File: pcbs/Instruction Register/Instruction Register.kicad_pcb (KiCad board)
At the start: 2 copper layers, 38 parts, among them J1001 Conn_02x20_Odd_Even, J1002 Conn_02x20_Odd_Even, U1001 74HC245, U1002 74HC245, U1003 74HC245, U1004 74HC245, U2001 74HC14, U2002 74HC08, U2003 74HC138, U3001 74HC245

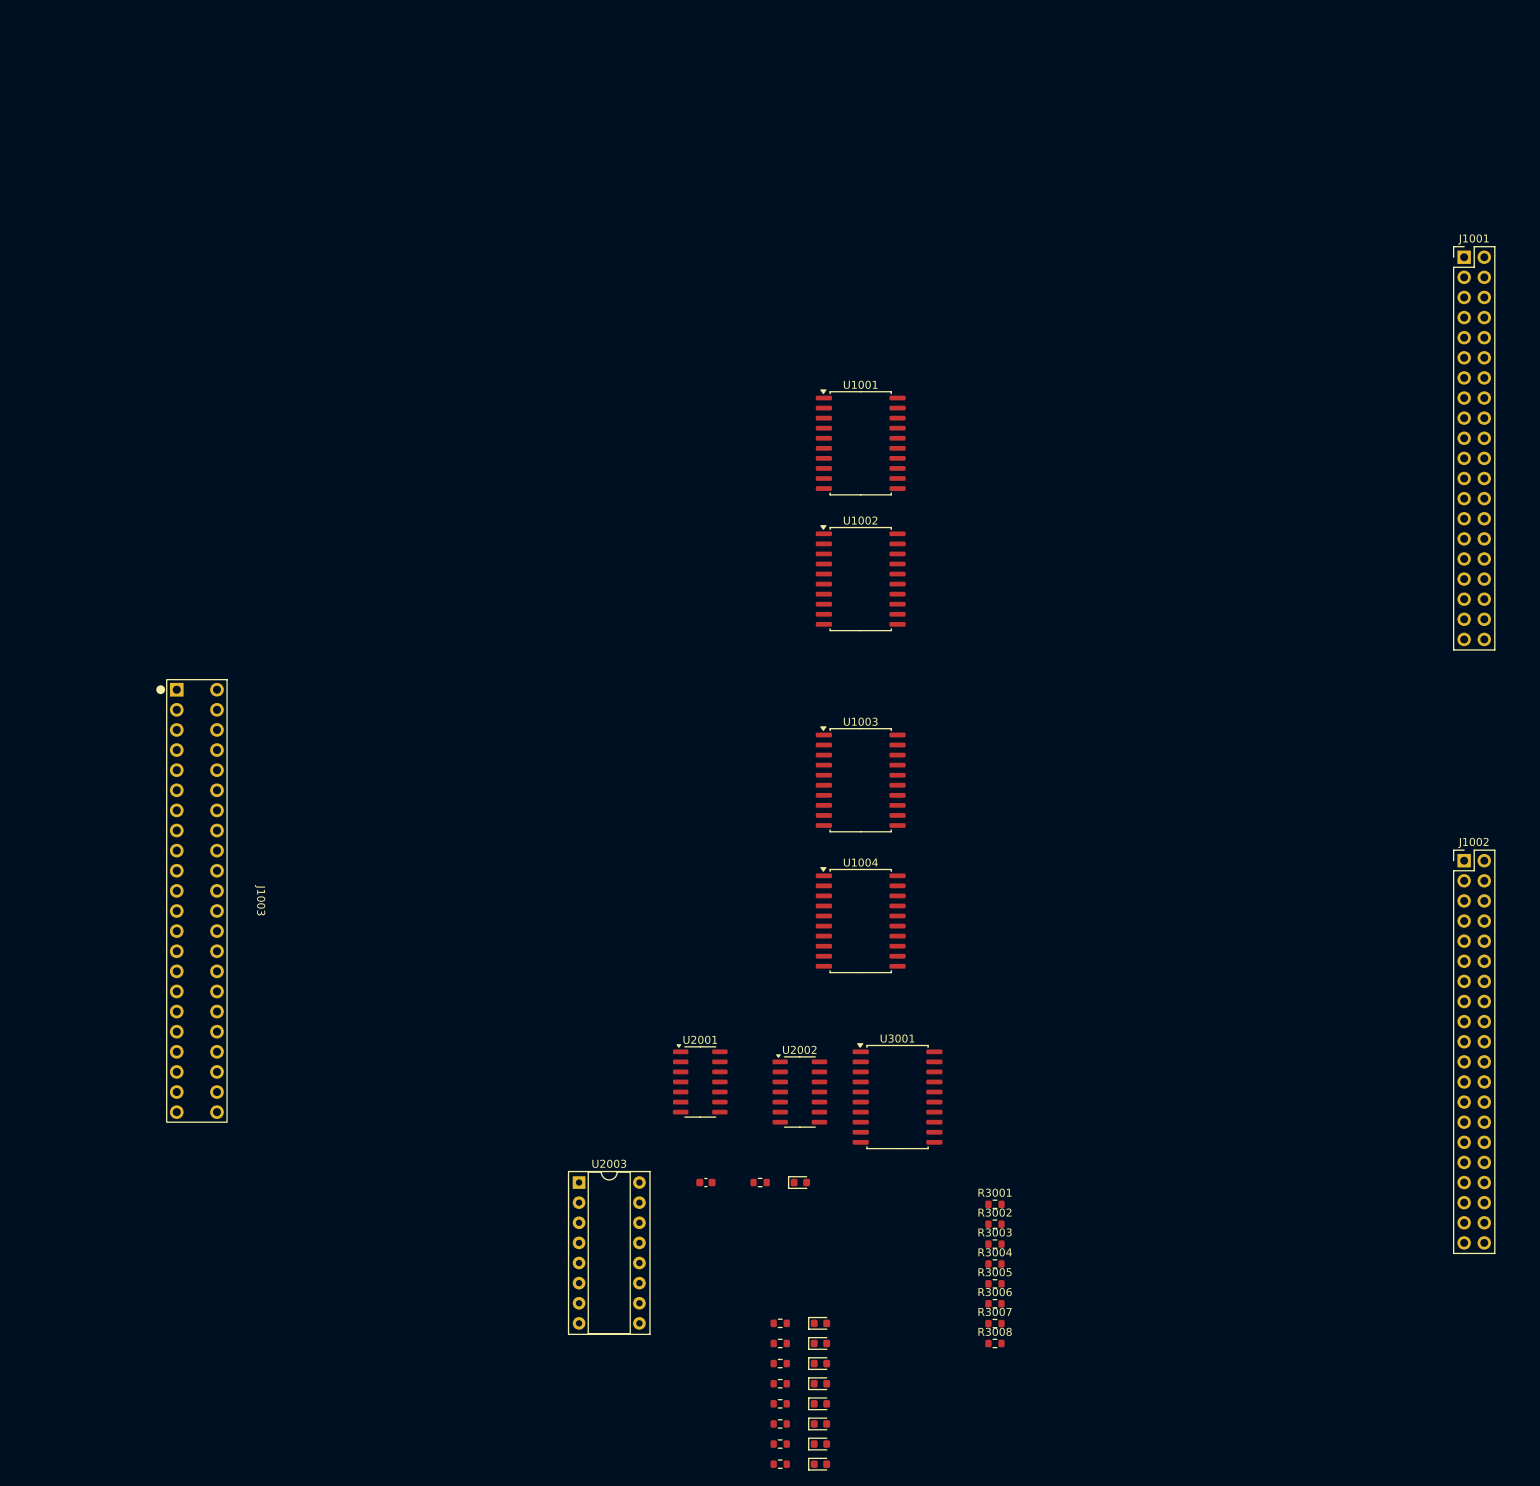
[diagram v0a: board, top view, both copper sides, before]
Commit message: Tweaking schematic and basic routing
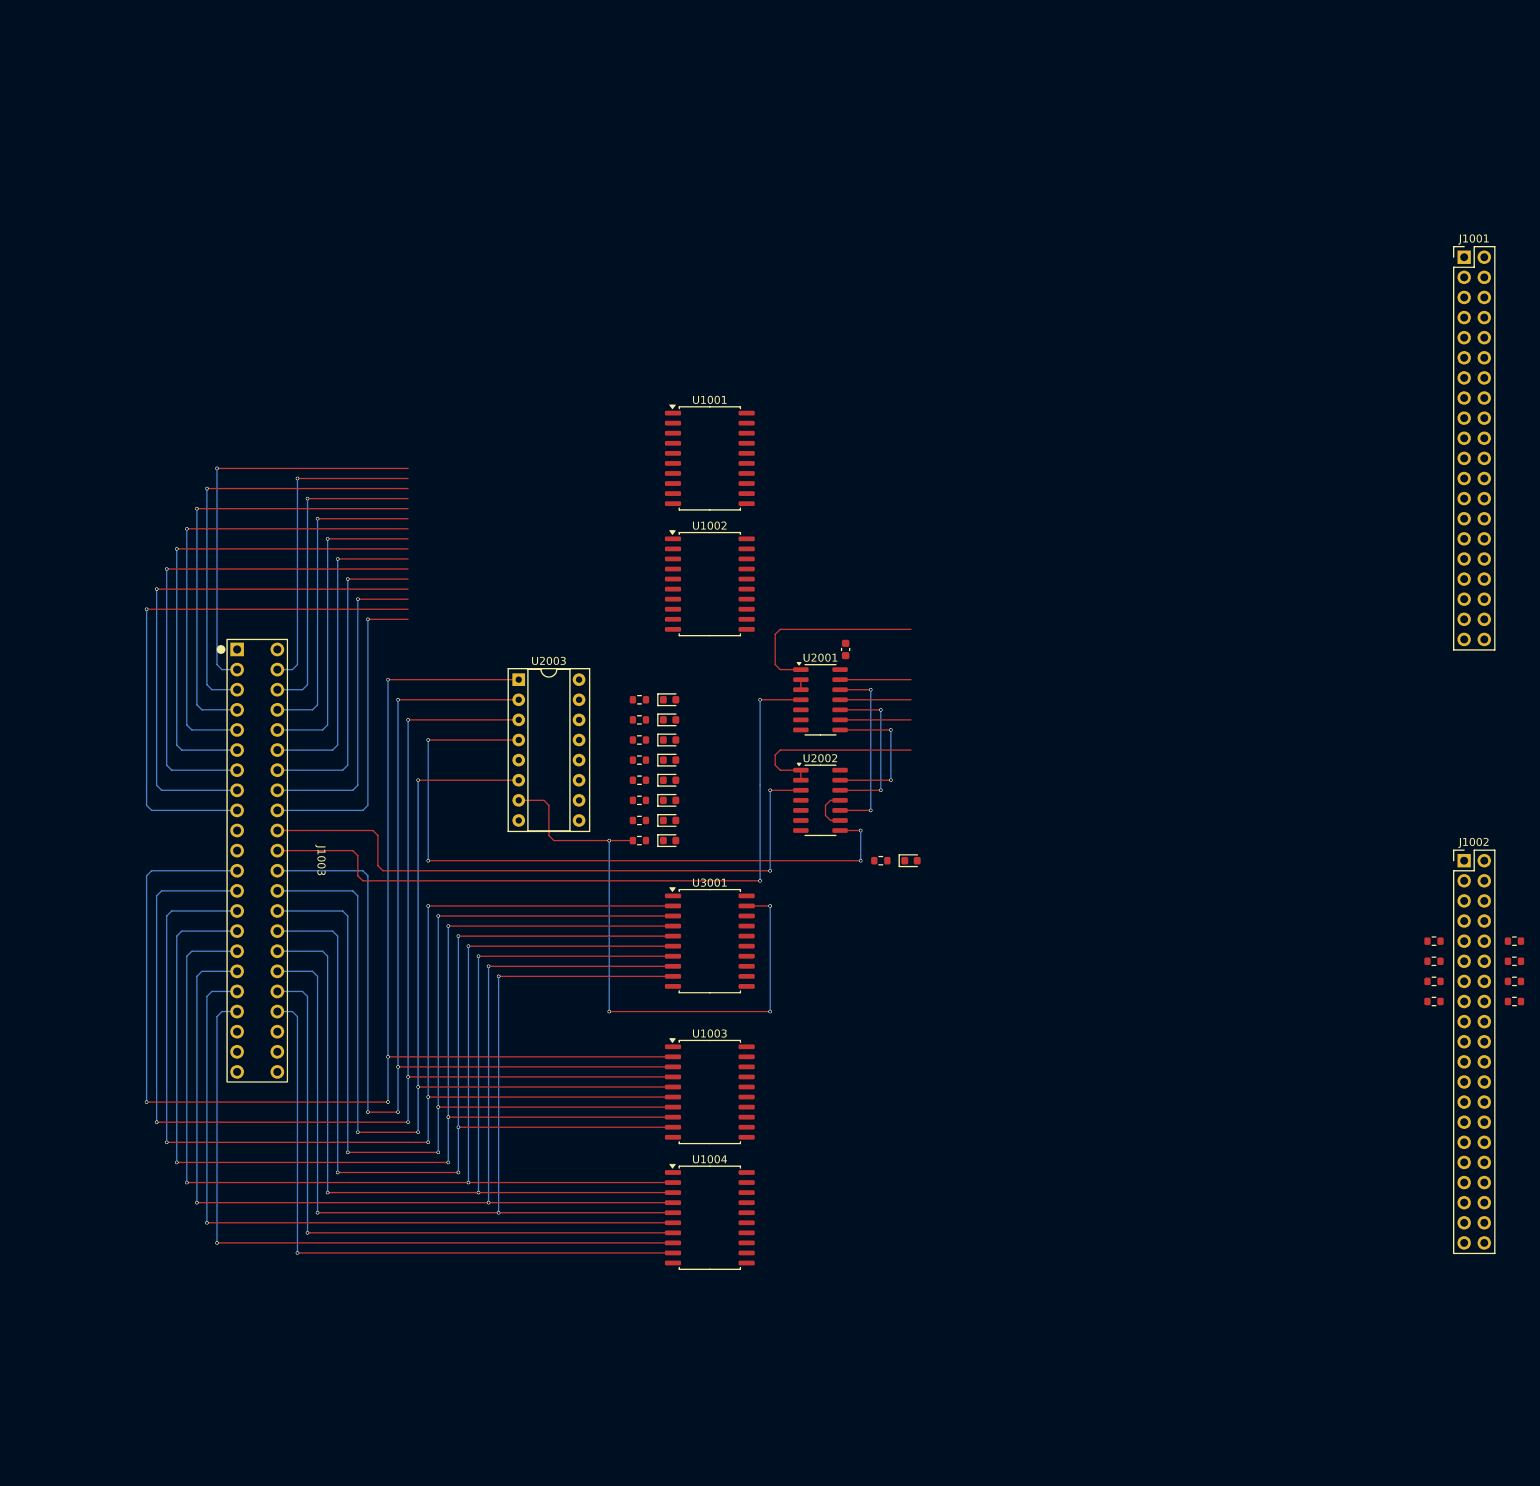
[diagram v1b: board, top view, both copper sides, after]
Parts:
- moved D2003 81.0 mm to (153.7, 109.2)
- moved D2006 81.0 mm to (153.7, 116.8)
- moved D2007 81.0 mm to (153.7, 119.4)
- moved D2004 81.0 mm to (153.7, 111.8)
- moved D2005 81.0 mm to (153.7, 114.3)
- moved D2008 81.0 mm to (153.7, 121.9)
- moved D2009 81.0 mm to (153.7, 124.5)
- moved D2002 81.0 mm to (153.7, 106.7)
- moved R2003 80.7 mm to (149.9, 109.2)
- moved R2006 80.7 mm to (149.9, 116.8)
- moved R2007 80.7 mm to (149.9, 119.4)
- moved R2004 80.7 mm to (149.9, 111.8)
- moved R2005 80.7 mm to (149.9, 114.3)
- moved R2008 80.7 mm to (149.9, 121.9)
- moved R2009 80.7 mm to (149.9, 124.5)
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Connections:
- J1003 pad B10: /~{RESET} -> /~{RESET}_{conn}
- U1001 pad 3: unconnected-(U1001-A1-Pad3) -> /Instr.In1
- U1001 pad 4: unconnected-(U1001-A2-Pad4) -> /Instr.In2
- U1001 pad 5: unconnected-(U1001-A3-Pad5) -> /Instr.In3
- U1001 pad 6: unconnected-(U1001-A4-Pad6) -> /Instr.In4
- U1001 pad 7: unconnected-(U1001-A5-Pad7) -> /Instr.In5
- U1001 pad 8: unconnected-(U1001-A6-Pad8) -> /Instr.In6
- U1001 pad 9: unconnected-(U1001-A7-Pad9) -> /Instr.In7
- U1002 pad 3: unconnected-(U1002-A1-Pad3) -> /Instr.In9
- U1002 pad 4: unconnected-(U1002-A2-Pad4) -> /Instr.In10
- U1002 pad 5: unconnected-(U1002-A3-Pad5) -> /Instr.In11
- U1002 pad 6: unconnected-(U1002-A4-Pad6) -> /Instr.In12
- U1002 pad 7: unconnected-(U1002-A5-Pad7) -> /Instr.In13
- U1002 pad 8: unconnected-(U1002-A6-Pad8) -> /Instr.In14
- U1002 pad 9: unconnected-(U1002-A7-Pad9) -> /Instr.In15
- U1003 pad 3: unconnected-(U1003-A1-Pad3) -> /Instr.Out1
- U1003 pad 4: unconnected-(U1003-A2-Pad4) -> /Instr.Out2
- U1003 pad 5: unconnected-(U1003-A3-Pad5) -> /Instr.Out3
- U1003 pad 6: unconnected-(U1003-A4-Pad6) -> /Instr.Out4
- U1003 pad 7: unconnected-(U1003-A5-Pad7) -> /Instr.Out5
- U1003 pad 8: unconnected-(U1003-A6-Pad8) -> /Instr.Out6
- U1003 pad 9: unconnected-(U1003-A7-Pad9) -> /Instr.Out7
- U1004 pad 3: unconnected-(U1004-A1-Pad3) -> /Instr.Out9
- U1004 pad 4: unconnected-(U1004-A2-Pad4) -> /Instr.Out10
- U1004 pad 5: unconnected-(U1004-A3-Pad5) -> /Instr.Out11
- U1004 pad 6: unconnected-(U1004-A4-Pad6) -> /Instr.Out12
- U1004 pad 7: unconnected-(U1004-A5-Pad7) -> /Instr.Out13
- U1004 pad 8: unconnected-(U1004-A6-Pad8) -> /Instr.Out14
- U1004 pad 9: unconnected-(U1004-A7-Pad9) -> /Instr.Out15
- U2002 pad 1: GND -> /~{RESET}
- U2002 pad 2: GND -> /~{RESET}
- U2002 pad 3: unconnected-(U2002-Pad3) -> /~{RESET}_{conn}
- U3001 pad 11: unconnected-(U3001-B7-Pad11) -> /C7
- U3001 pad 12: unconnected-(U3001-B6-Pad12) -> /C6
- U3001 pad 13: unconnected-(U3001-B5-Pad13) -> /C5
- U3001 pad 14: unconnected-(U3001-B4-Pad14) -> /C4
- U3001 pad 15: unconnected-(U3001-B3-Pad15) -> /C3
- U3001 pad 16: unconnected-(U3001-B2-Pad16) -> /C2
- U3001 pad 17: unconnected-(U3001-B1-Pad17) -> /C1
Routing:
- net /Instr.Out0: track 0.00 -> 176.6 mm, vias 0 -> 4
- net /Instr.Out2: track 0.00 -> 169.0 mm, vias 0 -> 4
- net /Instr.Out4: track 0.00 -> 162.4 mm, vias 0 -> 4
- net /Instr.Out6: track 0.00 -> 157.3 mm, vias 0 -> 4
- net /Instr.Out8: track 0.00 -> 152.3 mm, vias 0 -> 3
- net /Instr.Out1: track 0.00 -> 147.4 mm, vias 0 -> 4
- net /Instr.Out10: track 0.00 -> 147.2 mm, vias 0 -> 3
- net /Instr.Out5: track 0.00 -> 139.6 mm, vias 0 -> 4
- net /Instr.Out3: track 0.00 -> 137.2 mm, vias 0 -> 4
- net /Instr.Out7: track 0.00 -> 137.0 mm, vias 0 -> 4
- net /Instr.Out9: track 0.00 -> 134.5 mm, vias 0 -> 3
- net /Instr.Out11: track 0.00 -> 131.9 mm, vias 0 -> 3
- net /ClockInstr: track 0.00 -> 92.0 mm, vias 0 -> 2
- net /Instr.Out12: track 0.00 -> 91.5 mm, vias 0 -> 1
- net /Instr.Out14: track 0.00 -> 89.0 mm, vias 0 -> 1
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
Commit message: Completing routing; needs silkscreen
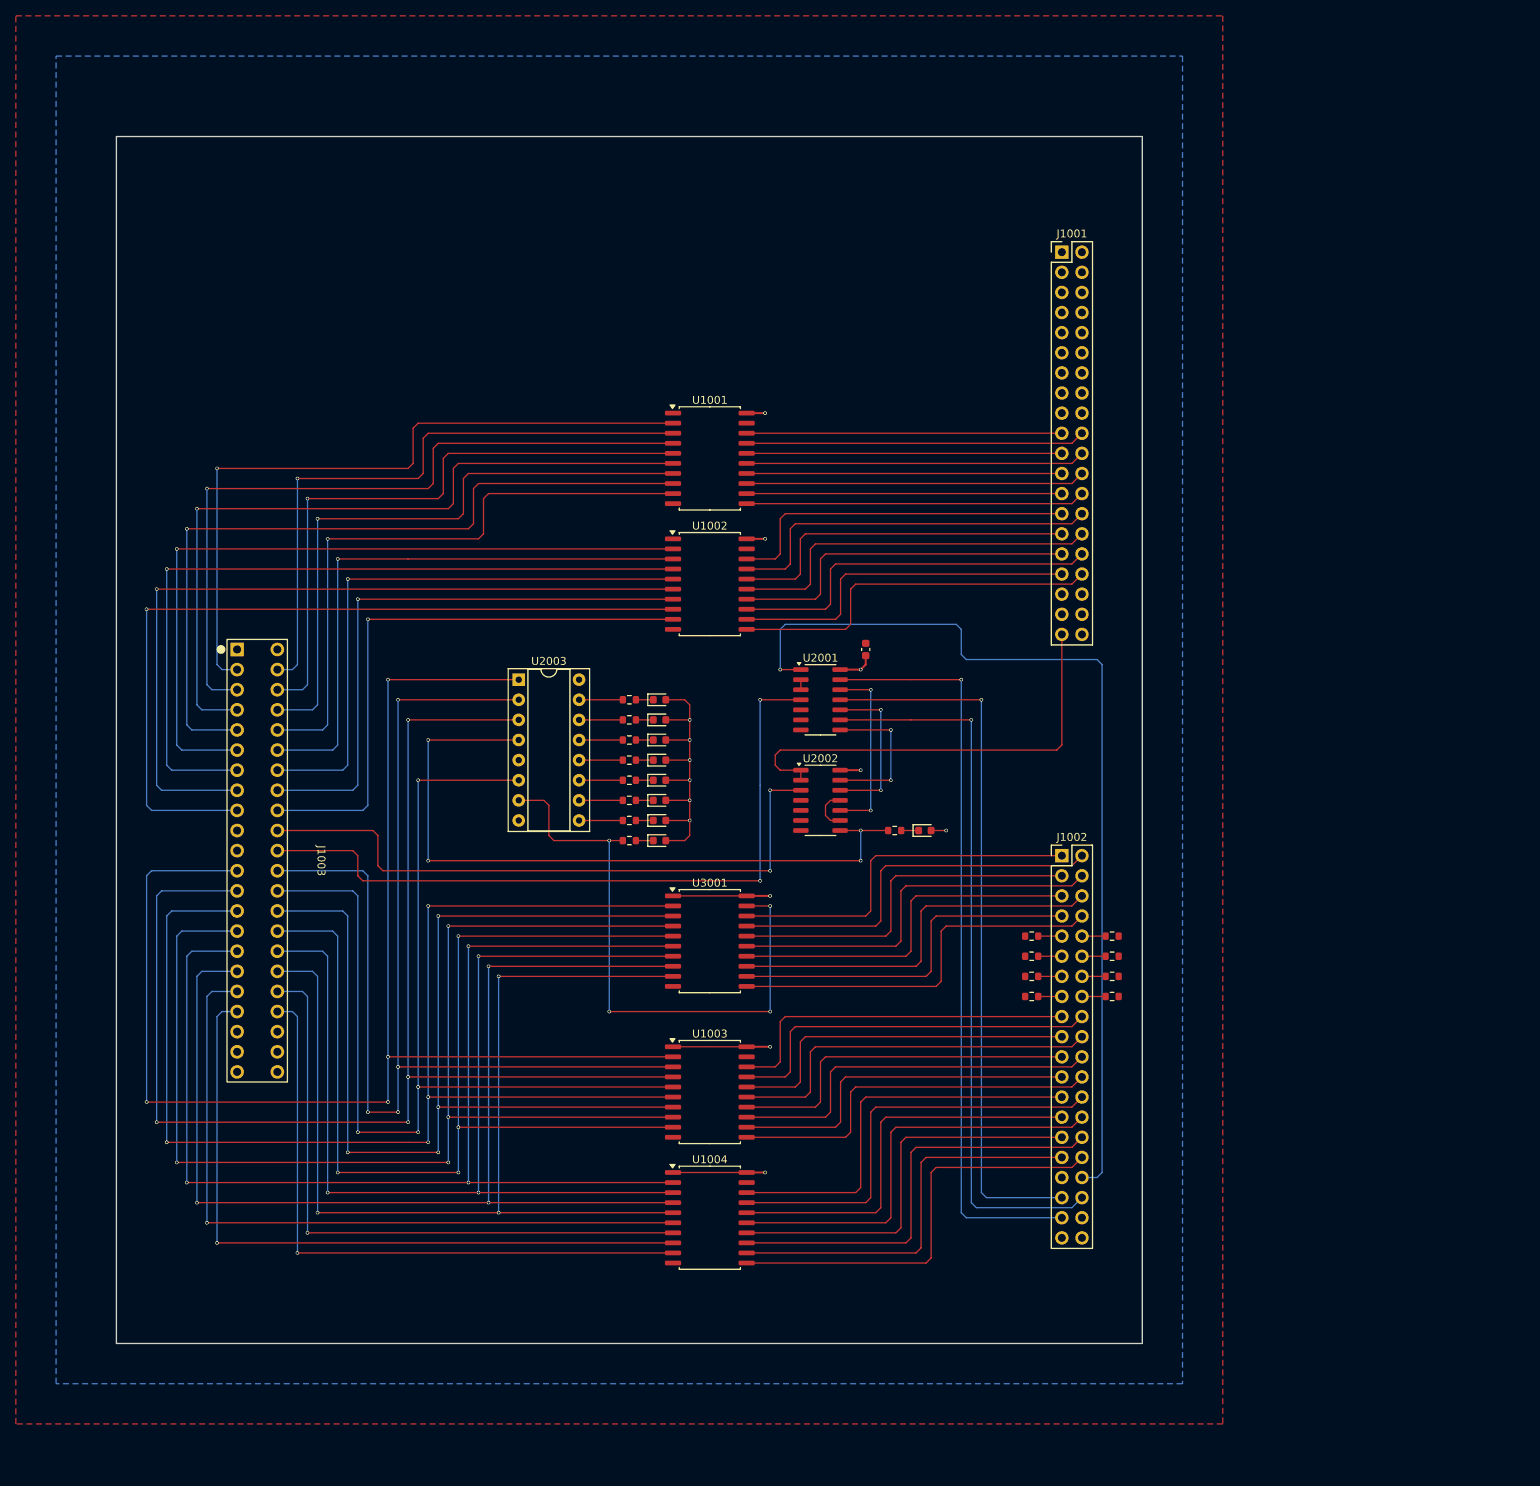
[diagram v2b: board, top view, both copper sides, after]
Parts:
- moved J1001 50.8 mm to (203.2, 50.2)
- moved J1002 50.8 mm to (203.2, 126.4)
- moved R3001 50.8 mm to (199.4, 136.5)
- moved R3002 50.8 mm to (209.6, 136.5)
- moved R3003 50.8 mm to (199.4, 139.1)
- moved R3004 50.8 mm to (209.6, 139.1)
- moved R3005 50.8 mm to (199.4, 141.6)
- moved R3006 50.8 mm to (209.6, 141.6)
- moved R3007 50.8 mm to (199.4, 144.1)
- moved R3008 50.8 mm to (209.6, 144.1)
- moved D2001 4.19 mm to (185.9, 123.2)
- moved R2001 4.19 mm to (182.1, 123.2)
- moved C2001 2.54 mm to (178.4, 100.3)
- moved R2002 1.27 mm to (148.6, 106.7)
- moved R2003 1.27 mm to (148.6, 109.2)
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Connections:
- U1001 pad 10: unconnected-(U1001-GND-Pad10) -> GND
- U1001 pad 11: unconnected-(U1001-B7-Pad11) -> /B7
- U1001 pad 12: unconnected-(U1001-B6-Pad12) -> /B6
- U1001 pad 13: unconnected-(U1001-B5-Pad13) -> /B5
- U1001 pad 14: unconnected-(U1001-B4-Pad14) -> /B4
- U1001 pad 15: unconnected-(U1001-B3-Pad15) -> /B3
- U1001 pad 16: unconnected-(U1001-B2-Pad16) -> /B2
- U1001 pad 17: unconnected-(U1001-B1-Pad17) -> /B1
- U1001 pad 20: unconnected-(U1001-VCC-Pad20) -> +5V
- U1002 pad 10: unconnected-(U1002-GND-Pad10) -> GND
- U1002 pad 11: unconnected-(U1002-B7-Pad11) -> /B15
- U1002 pad 12: unconnected-(U1002-B6-Pad12) -> /B14
- U1002 pad 13: unconnected-(U1002-B5-Pad13) -> /B13
- U1002 pad 14: unconnected-(U1002-B4-Pad14) -> /B12
- U1002 pad 15: unconnected-(U1002-B3-Pad15) -> /B11
- U1002 pad 16: unconnected-(U1002-B2-Pad16) -> /B10
- U1002 pad 17: unconnected-(U1002-B1-Pad17) -> /B9
- U1002 pad 20: unconnected-(U1002-VCC-Pad20) -> +5V
- U1003 pad 10: unconnected-(U1003-GND-Pad10) -> GND
- U1003 pad 20: unconnected-(U1003-VCC-Pad20) -> +5V
- U1004 pad 10: unconnected-(U1004-GND-Pad10) -> GND
- U1004 pad 20: unconnected-(U1004-VCC-Pad20) -> +5V
- U3001 pad 20: unconnected-(U3001-VCC-Pad20) -> +5V
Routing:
- net /Cycle1: track 24.7 -> 119.5 mm, vias 0 -> 1
- net +5V: track 0.00 -> 91.2 mm, vias 0 -> 14
- net /Cycle4: track 8.96 -> 95.6 mm, vias 0 -> 1
- net /Cycle3: track 8.96 -> 92.3 mm, vias 0 -> 1
- net /Cycle2: track 8.96 -> 90.5 mm, vias 0 -> 1
- net /R_{C}3: track 0.00 -> 54.2 mm
- net /R_{B}3: track 0.00 -> 54.2 mm
- net /R_{B}1: track 0.00 -> 54.2 mm
- net /R_{C}1: track 0.00 -> 54.2 mm
- net /R_{C}2: track 0.00 -> 51.1 mm
- net /R_{C}0: track 0.00 -> 51.1 mm
- net /R_{B}2: track 0.00 -> 51.1 mm
- net /R_{B}0: track 0.00 -> 51.1 mm
- net /C5: track 0.00 -> 49.7 mm
- net /C1: track 0.00 -> 49.7 mm
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- added copper zone on B.Cu, net +5V
- added copper zone on F.Cu, net GND
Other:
- board outline added: 129.5 x 152.4 mm

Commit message: Preliminary final layout
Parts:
- added H1001: MountingHole, MountingHole:MountingHole_2.7mm_M2.5_ISO7380, F.Cu at (91.4, 43.2)
- added H1002: MountingHole, MountingHole:MountingHole_2.7mm_M2.5_ISO7380, F.Cu at (205.7, 43.2)
- added H1003: MountingHole, MountingHole:MountingHole_2.7mm_M2.5_ISO7380, F.Cu at (205.7, 180.3)
- added H1004: MountingHole, MountingHole:MountingHole_2.7mm_M2.5_ISO7380, F.Cu at (91.4, 180.3)
- moved D2002 2.54 mm to (149.9, 106.7)
- moved D2003 2.54 mm to (149.9, 109.2)
- moved D2004 2.54 mm to (149.9, 111.8)
- moved D2005 2.54 mm to (149.9, 114.3)
- moved D2006 2.54 mm to (149.9, 116.8)
- moved D2007 2.54 mm to (149.9, 119.4)
- moved D2008 2.54 mm to (149.9, 121.9)
- moved D2009 2.54 mm to (149.9, 124.5)
- moved R2002 2.54 mm to (146.1, 106.7)
- moved R2003 2.54 mm to (146.1, 109.2)
- moved R2004 2.54 mm to (146.1, 111.8)
- moved R2005 2.54 mm to (146.1, 114.3)
- moved R2006 2.54 mm to (146.1, 116.8)
- moved R2007 2.54 mm to (146.1, 119.4)
- moved R2008 2.54 mm to (146.1, 121.9)
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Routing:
- net +5V: track 91.2 -> 111.5 mm
- net /Control/~{StoreW}: track 5.52 -> 2.98 mm
- net /Control/~{StoreB}: track 5.52 -> 2.98 mm
- net /Control/~{LoadW}: track 5.52 -> 2.98 mm
- net /Control/~{LoadPC}: track 5.52 -> 2.98 mm
- net /Control/~{LoadB}: track 5.52 -> 2.98 mm
- net /Control/~{Halt}: track 5.52 -> 2.98 mm
- net /Control/~{BranchZero}: track 5.52 -> 2.98 mm
- net /~{Set}: track 75.7 -> 77.0 mm
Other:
- board text added: "+5V"
- board text added: "ACTIVE"
- board text added: "BRANCHZERO"
- board text added: "GND"
- board text added: "HALT"
- board text added: "Instruction Register"
- board text added: "JLCJLCJLCJLC"
- board text added: "LOADB"
- board text added: "LOADPC"
- board text added: "LOADW"
- board text added: "SET"
- board text added: "STOREB"
- board text added: "STOREW"
